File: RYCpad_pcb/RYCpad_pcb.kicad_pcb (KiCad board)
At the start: 2 copper layers, 77.2 x 117.6 mm, 67 parts, among them J1 USB_C_Receptacle_USB2.0, J2 AVR ISP, K1 KEYSW, K10 KEYSW, K11 KEYSW, K12 KEYSW, K13 KEYSW, K14 KEYSW, K15 KEYSW, K16 KEYSW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

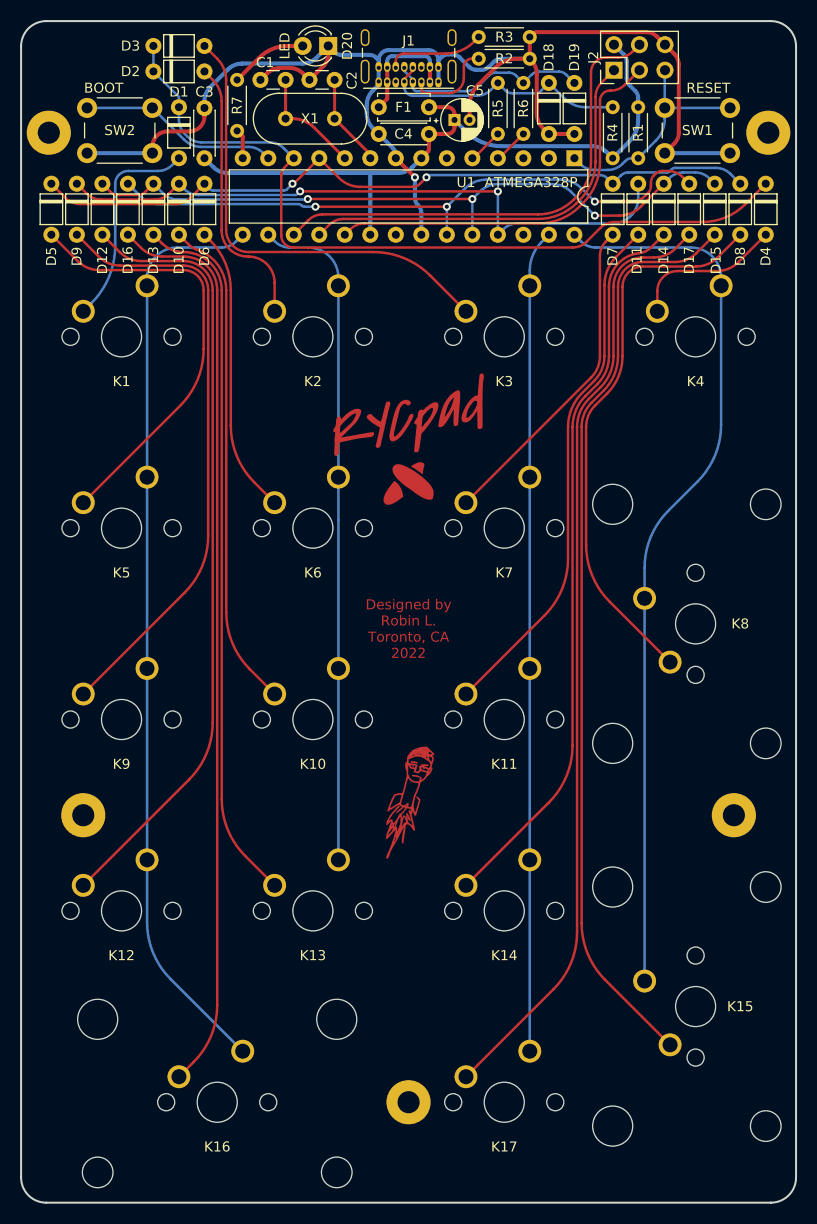
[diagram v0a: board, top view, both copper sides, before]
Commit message: added copper trim
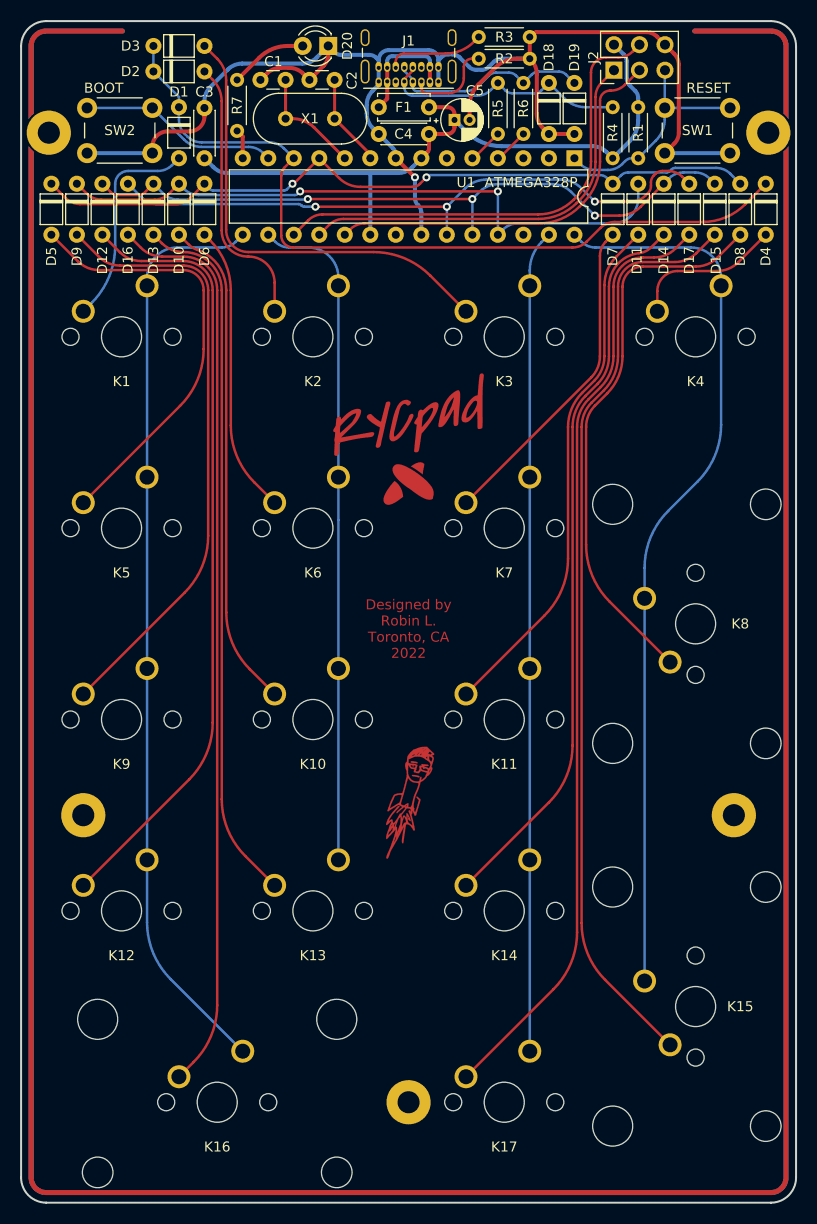
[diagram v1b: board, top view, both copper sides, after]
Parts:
- added svg2mod: G***, personal:RYCpad_coppertrim, F.Cu at (0.00, -1.20)
- added svg2mod: G***, personal:RYCpad_coppertrim, B.Cu at (0.00, -1.20)

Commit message: add version number to pcb
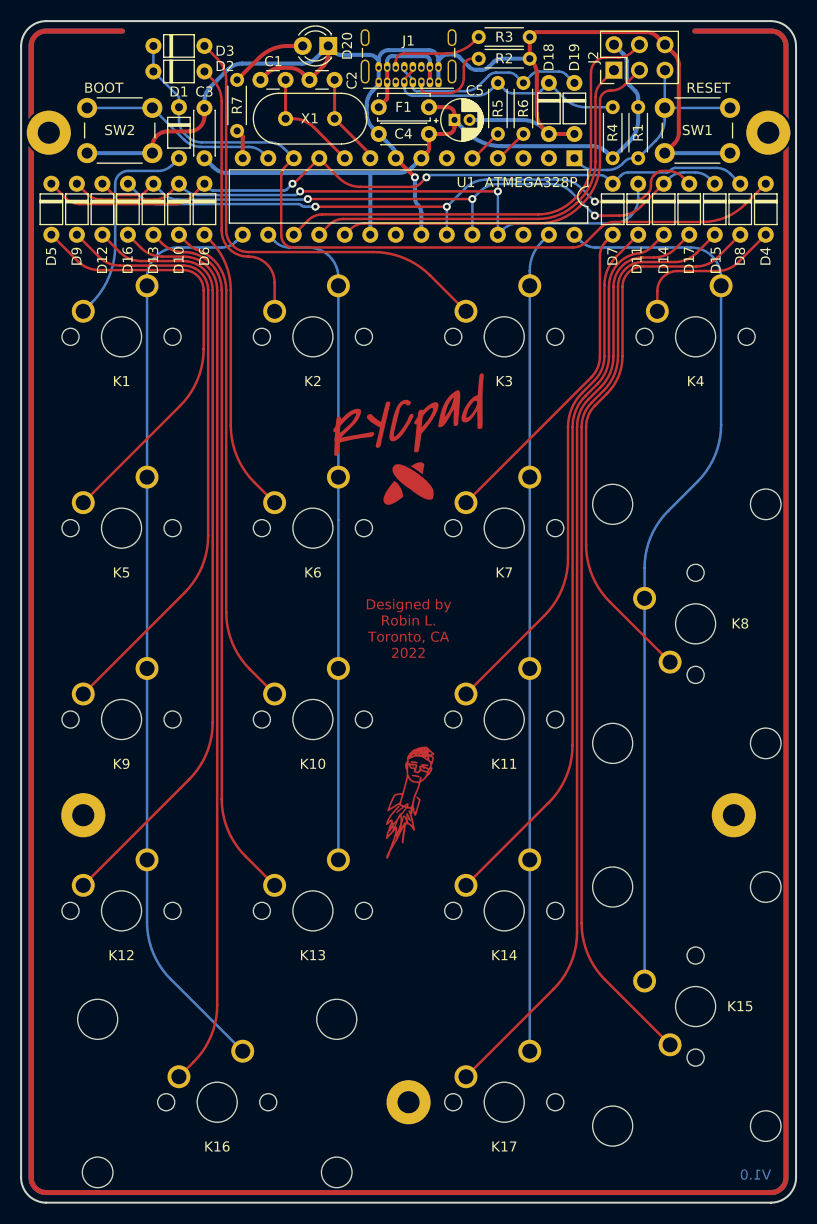
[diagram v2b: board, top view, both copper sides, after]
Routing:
- net GND: track 139.6 -> 138.1 mm
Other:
- board text added: "V1.0"
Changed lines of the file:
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@@
     (property "Sheetname" "")
     (attr through_hole)
-    (fp_text reference "D2" (at -2.286 0) (layer "F.SilkS")
+    (fp_text reference "D2" (at 7.112 -0.508) (layer "F.SilkS")
       (effects (font (size 1 1) (thickness 0.15)))
     )
@@
     (property "Sheetname" "")
     (attr through_hole)
-    (fp_text reference "D3" (at -2.286 0) (layer "F.SilkS")
+    (fp_text reference "D3" (at 7.112 0.508) (layer "F.SilkS")
       (effects (font (size 1 1) (thickness 0.15)))
     )
@@
     (effects (font (size 1 1) (thickness 0.175)))
   )
+  (gr_text "V1.0" (at 34.544 54.864) (layer "B.Cu")
+    (effects (font (size 1 1) (thickness 0.175)) (justify mirror))
+  )
   (gr_text "1" (at -28.575 33.02) (layer "B.SilkS")
     (effects (font (size 1.5 1.5) (thickness 0.3)) (justify mirror))
@@
   (segment (start 13.97 -48.768) (end 16.51 -48.768) (width 0.4) (layer "F.Cu") (net 23))
   (segment (start 0.635 -44.45) (end -1.27 -46.355) (width 0.4) (layer "F.Cu") (net 23))
-  (segment (start 6.072 -50.165) (end 6.072 -51.565359) (width 0.4) (layer "F.Cu") (net 23))
   (segment (start 26.903511 -48.883831) (end 26.903511 -55.660169) (width 0.4) (layer "F.Cu") (net 23))
   (segment (start 13.350787 -49.387213) (end 13.97 -48.768) (width 0.4) (layer "F.Cu") (net 23))
@@
   (segment (start -24.004 -49.022) (end -21.82 -49.022) (width 0.4) (layer "F.Cu") (net 23))
   (segment (start 12.765 -54.732573) (end 12.765 -50.801427) (width 0.4) (layer "F.Cu") (net 23))
-  (segment (start 6.95068 -53.68668) (end 8.646321 -55.382321) (width 0.4) (layer "F.Cu") (net 23))
   (segment (start -9.866 -54.1528) (end -8.44034 -55.57846) (width 0.4) (layer "F.Cu") (net 23))
   (segment (start -8.001 -56.63912) (end -8.001 -57.531) (width 0.4) (layer "F.Cu") (net 23))
@@
   (segment (start -25.504 -46.863) (end -25.504 -47.522) (width 0.4) (layer "F.Cu") (net 23))
   (segment (start 23.656169 -58.907511) (end 12.759618 -58.907511) (width 0.4) (layer "F.Cu") (net 23))
-  (segment (start 10.767641 -56.261) (end 12.065 -56.261) (width 0.4) (layer "F.Cu") (net 23))
   (segment (start 12.406064 -58.761064) (end 12.065 -58.42) (width 0.4) (layer "F.Cu") (net 23))
   (via (at 0.635 -44.45) (size 0.8) (drill 0.4) (layers "F.Cu" "B.Cu") (net 23))
-  (arc (start 6.072 -51.565359) (mid 6.300362 -52.71341) (end 6.95068 -53.68668) (width 0.4) (layer "F.Cu") (net 23))
-  (arc (start 10.767641 -56.261) (mid 9.619591 -56.032639) (end 8.646321 -55.382321) (width 0.4) (layer "F.Cu") (net 23))
   (arc (start 23.656169 -58.907511) (mid 24.230194 -58.79333) (end 24.716829 -58.468171) (width 0.4) (layer "F.Cu") (net 23))
   (arc (start 12.765 -50.801427) (mid 12.917241 -50.03606) (end 13.350787 -49.387213) (width 0.4) (layer "F.Cu") (net 23))
@@
   (segment (start -2.975 -54) (end -2.975 -55.35) (width 0.4) (layer "B.Cu") (net 23))
   (segment (start 0.635 -44.45) (end 0.635 -42.400414) (width 0.4) (layer "B.Cu") (net 23))
+  (segment (start 13.45168 -49.28632) (end 13.97 -48.768) (width 0.4) (layer "B.Cu") (net 23))
   (segment (start -8.001 -57.531) (end -7.404893 -56.934893) (width 0.4) (layer "B.Cu") (net 23))
   (segment (start 1.27 -40.936986) (end 1.27 -38.735) (width 0.4) (layer "B.Cu") (net 23))
@@
   (segment (start -6.697786 -56.642) (end -3.916694 -56.642) (width 0.4) (layer "B.Cu") (net 23))
   (segment (start 2.975 -56.11452) (end 2.975 -55.35) (width 0.4) (layer "B.Cu") (net 23))
+  (segment (start 6.072 -50.165) (end 11.330359 -50.165) (width 0.4) (layer "B.Cu") (net 23))
   (segment (start 4.360986 -56.6928) (end 3.967494 -56.6928) (width 0.4) (layer "B.Cu") (net 23))
   (segment (start -9.167813 -56.364187) (end -8.001 -57.531) (width 0.4) (layer "B.Cu") (net 23))
@@
   (arc (start 3.967494 -56.6928) (mid 3.584811 -56.61668) (end 3.260387 -56.399907) (width 0.4) (layer "B.Cu") (net 23))
   (arc (start 6.720725 -55.161489) (mid 6.338042 -55.237609) (end 6.013618 -55.454382) (width 0.4) (layer "B.Cu") (net 23))
+  (arc (start 11.330359 -50.165) (mid 12.47841 -49.936638) (end 13.45168 -49.28632) (width 0.4) (layer "B.Cu") (net 23))
   (arc (start 2.975 -56.11452) (mid 2.682107 -56.821627) (end 1.975 -57.11452) (width 0.4) (layer "B.Cu") (net 23))
   (arc (start -6.697786 -56.642) (mid -7.080469 -56.71812) (end -7.404893 -56.934893) (width 0.4) (layer "B.Cu") (net 23))

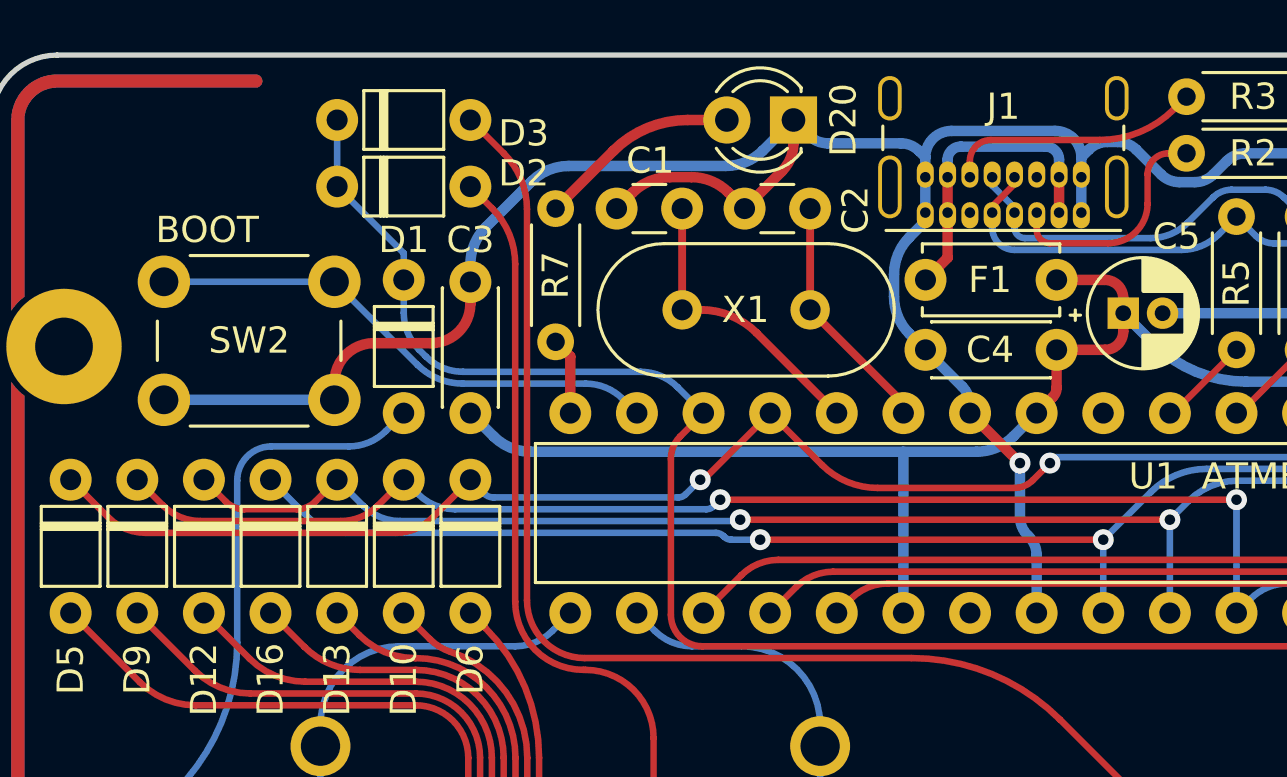
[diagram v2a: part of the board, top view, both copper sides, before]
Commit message: connected shield through RC filter
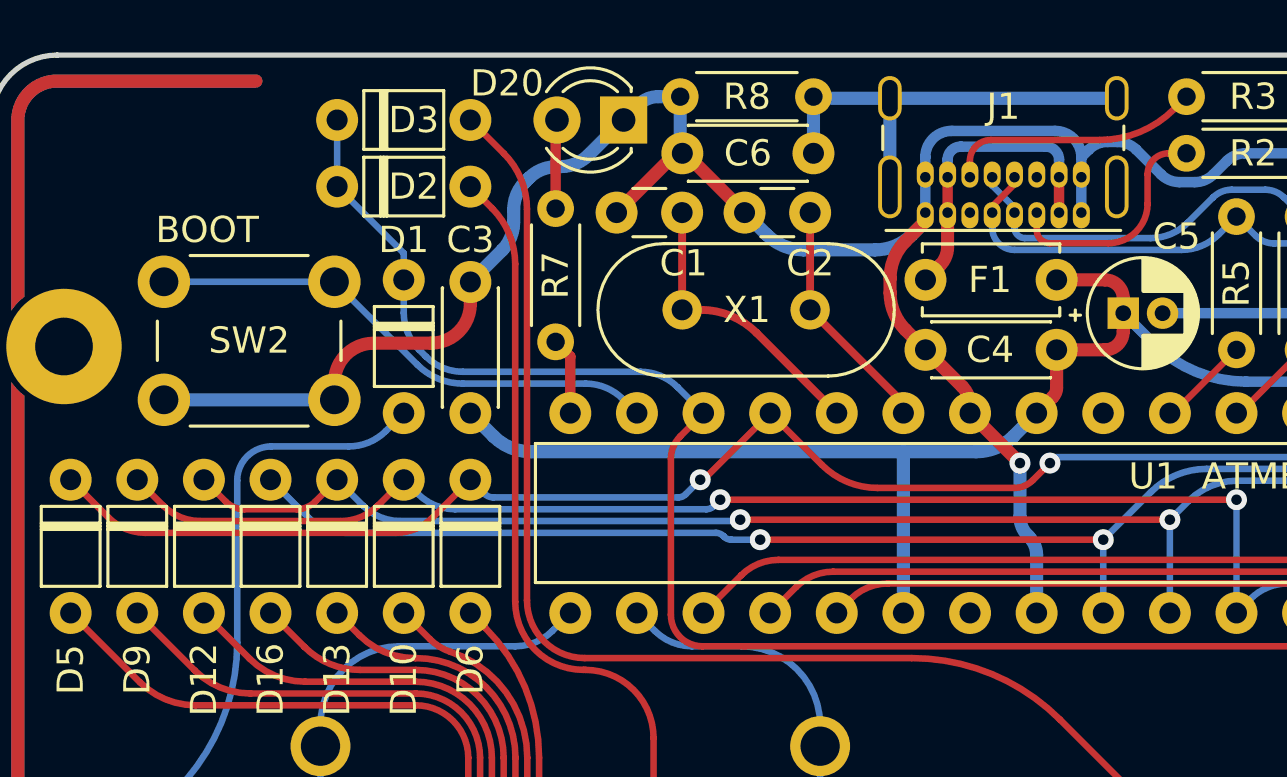
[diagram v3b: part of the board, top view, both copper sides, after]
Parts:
- added C6: 0.1u, Capacitor_THT:C_Disc_D4.3mm_W1.9mm_P5.00mm, F.Cu at (-7.24, -56.3)
- added R8: 330, Resistor_THT:R_Axial_DIN0204_L3.6mm_D1.6mm_P5.08mm_Horizontal, F.Cu at (-7.24, -58.4)
- moved D20 6.48 mm to (-14.5, -57.5)
- moved C1 0.15 mm to (-12.2, -54.0)
- moved C2 0.15 mm to (-7.37, -54.0)
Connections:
- J1 pad S1: unconnected-(J1-PadS1) -> Net-(J1-PadS1)
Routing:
- net Net-(J1-PadS1): track 0.00 -> 17.1 mm
- net Net-(D20-Pad2): track 7.74 -> 3.40 mm
- net GND: track 138.1 -> 136.1 mm

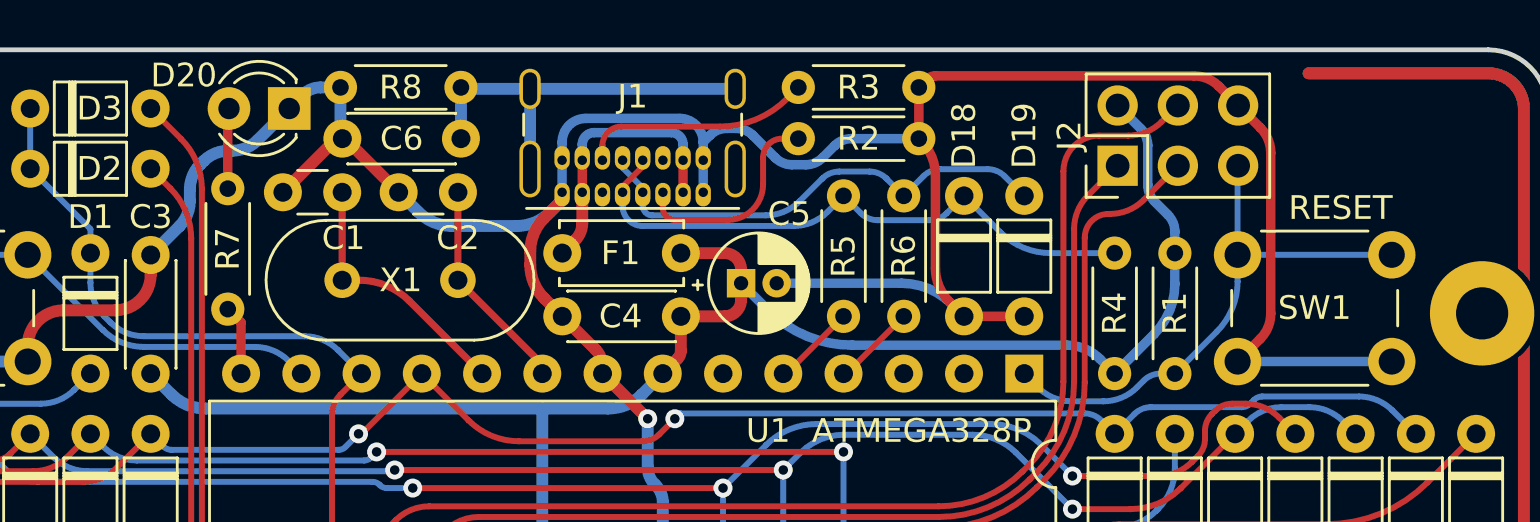
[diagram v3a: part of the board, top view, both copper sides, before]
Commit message: thickened power traces
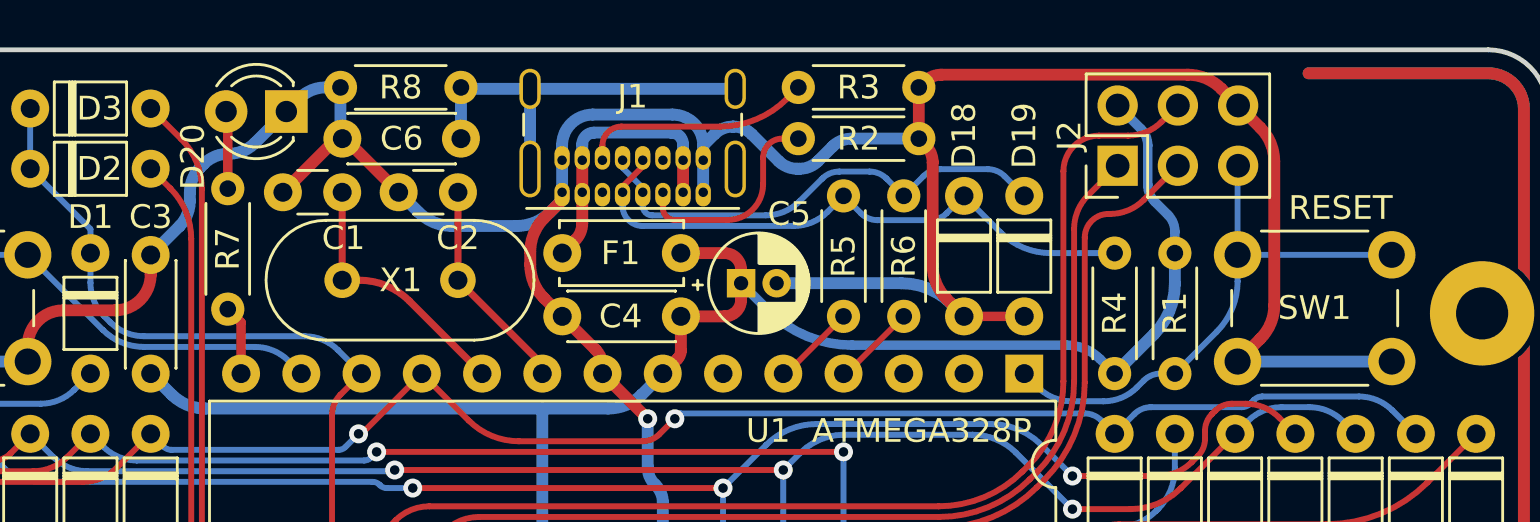
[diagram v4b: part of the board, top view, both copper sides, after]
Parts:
- moved D20 0.18 mm to (-14.6, -57.4)
